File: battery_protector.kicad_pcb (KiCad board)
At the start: 4 copper layers, 93.7 x 93.8 mm, 104 parts, among them J1 TB005-762-02BE, J2 TB005-762-02BE, J3 USB_C_Receptacle_USB2.0_16P, J5 Conn_01x12, Q1 SQJQ184ER, Q2 SQJQ184ER, Q3 SQJQ184ER, Q4 SQJQ184ER, Q5 MMBT3904, Q6 MMBT3904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

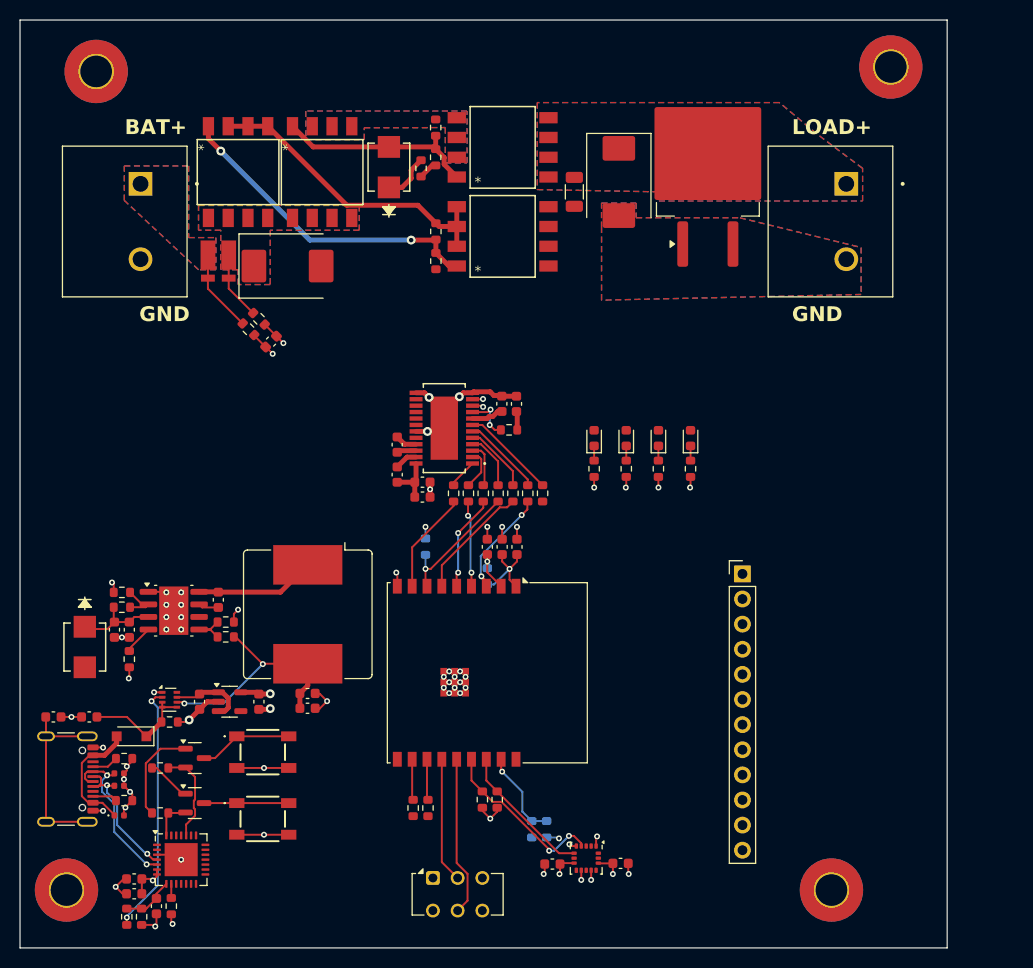
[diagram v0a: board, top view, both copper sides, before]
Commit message: Nima/aug 16 (#7)
* Routed Gate Driver, will have to move all components to top layer for simplicity and move the switching reg farther away from the mcu

* More routing, changed the footprints of some caps.
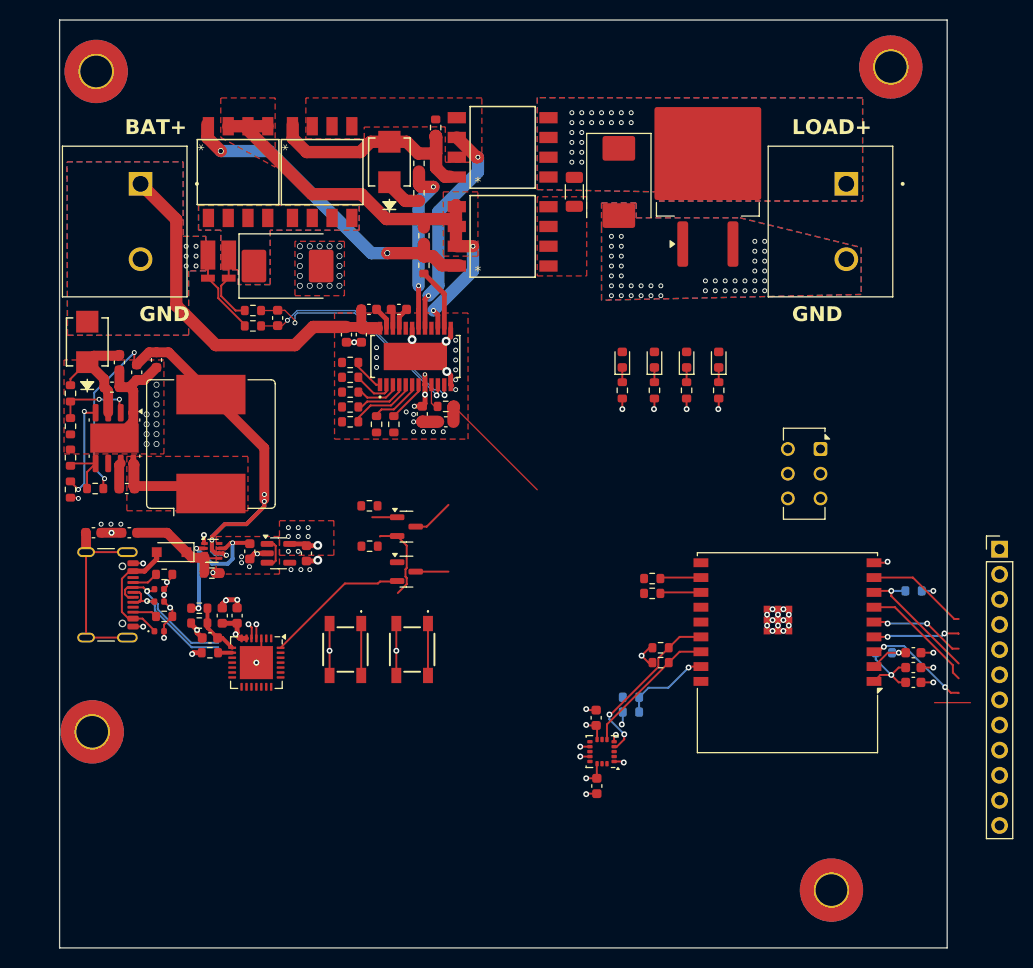
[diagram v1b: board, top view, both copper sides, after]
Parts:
- moved SW1 58.5 mm to (154.6, 100.5), turned to -90 degrees
- moved R25 49.6 mm to (164.1, 114.8), turned to 180 degrees
- moved C14 44.4 mm to (164.0, 121.1), turned to 0 degrees
- moved C12 43.3 mm to (164.0, 122.6), turned to 0 degrees
- moved C13 42.4 mm to (164.0, 124.1), turned to 0 degrees
- moved R27 40.8 mm to (161.1, 121.1), turned to 0 degrees
- moved C8 38.1 mm to (85.5, 92.8), turned to -90 degrees
- moved C7 37.0 mm to (87.5, 91.5), turned to -90 degrees
- moved R30 34.3 mm to (109.0, 110.3)
- moved R31 33.9 mm to (109.0, 106.3)
- moved R33 33.5 mm to (137.6, 113.6), turned to 0 degrees
- moved U5 33.1 mm to (150.8, 118.3), turned to 180 degrees
- moved R23 32.0 mm to (91.8, 116.6), turned to 0 degrees
- moved Q5 31.7 mm to (112.8, 108.4)
- moved Q6 31.7 mm to (112.8, 112.9)
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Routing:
- net +5V0_board: track 23.9 -> 61.0 mm, vias 2 -> 6
- net BAT+: track 13.6 -> 47.1 mm, vias 0 -> 6
- net /GateDriver/SOURCE_A: track 0.00 -> 22.5 mm, vias 0 -> 2
- net /GateDriver/IS_N: track 3.79 -> 23.9 mm
- net /GateDriver/IS_P: track 3.77 -> 23.8 mm
- net Net-(SW1B-B): track 16.2 -> 0.00 mm
- net /GateDriver/GATE_A: track 1.94 -> 17.7 mm, vias 0 -> 2
- net /MCU/GD_IS: track 1.89 -> 17.1 mm
- net /GateDriver/SOURCE_B: track 31.3 -> 45.5 mm, vias 0 -> 2
- net Net-(SW1A-B): track 12.7 -> 0.00 mm
- net +5V0: track 33.2 -> 20.6 mm, vias 2 -> 3
- net /MCU/DTR: track 3.95 -> 14.4 mm
- net Net-(U1-RT): track 2.97 -> 10.5 mm, vias 0 -> 2
- net Net-(Q5-B): track 9.90 -> 2.52 mm
- net /GateDriver/GATE_B: track 0.00 -> 6.39 mm
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- added copper zone on F.Cu, net +3V3
- added copper zone on F.Cu, net +5V0
- added copper zone on F.Cu, net /GateDriver/SOURCE_B
- added copper zone on F.Cu, net Net-(Q3-D)
- added copper zone on F.Cu, net Net-(U1-SW)
- removed copper zone on B.Cu, net /GateDriver/SOURCE_A
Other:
- board size 93.7 x 93.8 mm -> 89.7 x 93.8 mm
